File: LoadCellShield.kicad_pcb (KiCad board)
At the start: 2 copper layers, 68.6 x 53.3 mm, 34 parts, among them IC1 INA125, IC2 INA125, J1 Screw_Terminal_01x04, J2 Screw_Terminal_01x04, J7 Barrel_Jack_Switch, P1 Power, P2 Analog, P3 Digital, P4 Digital, P5 CONN_01X01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

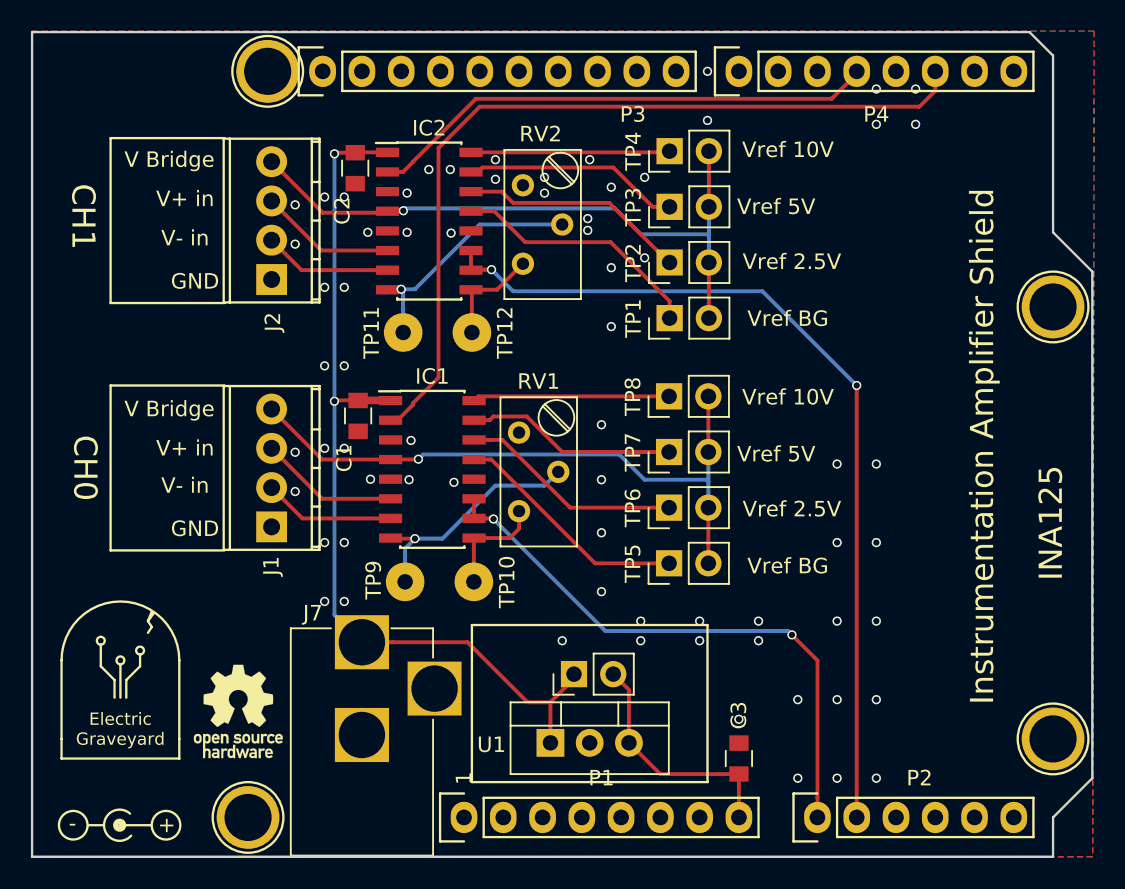
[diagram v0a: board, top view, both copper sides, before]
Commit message: Revise Layout to simplify build
Assembling these was a pain because of the 8x 2 position headers.  Squashed them so 2x 8 position ones will work.  Also some improvements to general routing.
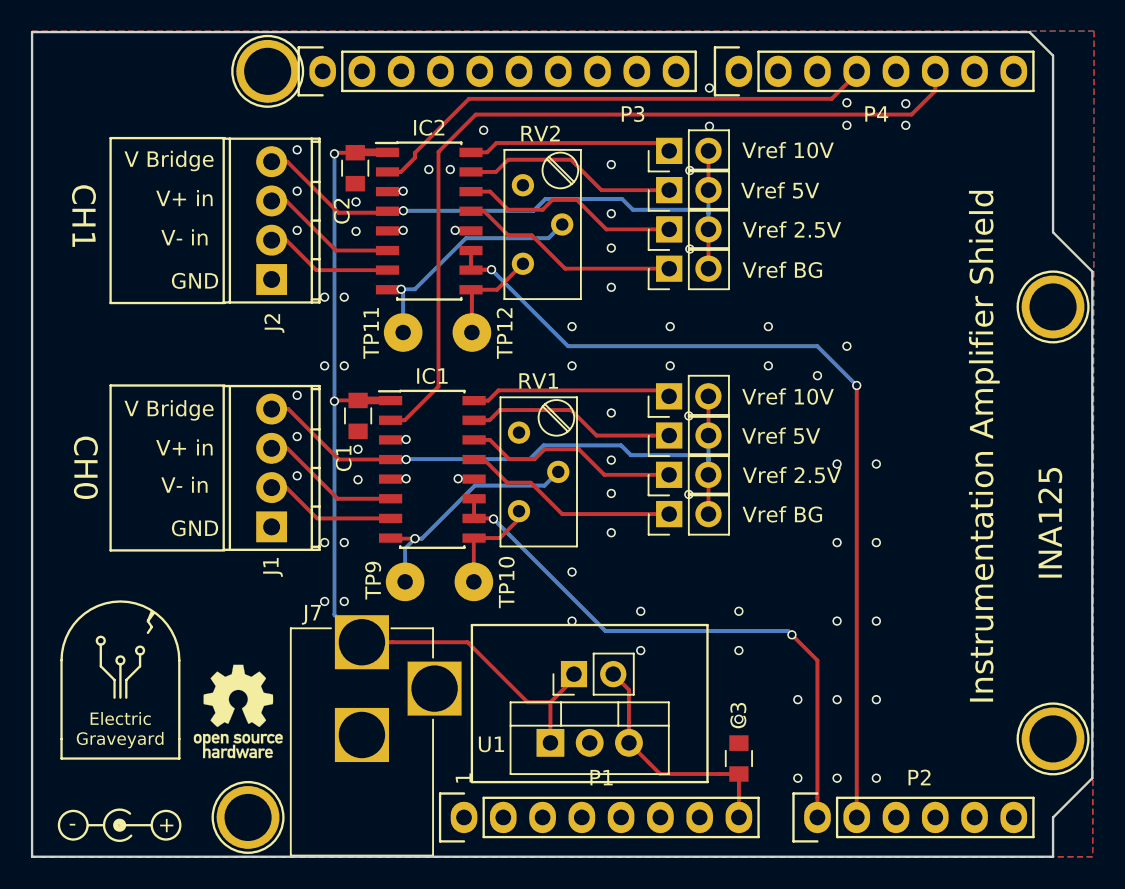
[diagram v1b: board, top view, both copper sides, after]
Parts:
- moved TP1 3.20 mm to (152.2, 88.3)
- moved TP5 3.18 mm to (152.2, 104.2)
- moved TP2 2.14 mm to (152.2, 85.8)
- moved TP6 2.12 mm to (152.2, 101.7)
- moved TP3 1.08 mm to (152.2, 83.2)
- moved TP7 1.06 mm to (152.2, 99.1)
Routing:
- net V_Bridge1: track 41.3 -> 38.2 mm
- net V_Bridge0: track 41.3 -> 39.2 mm
- net Net-(IC2-Pad13): track 16.8 -> 14.8 mm
- net Net-(IC1-Pad13): track 15.8 -> 14.5 mm
- net Net-(IC2-Pad16): track 13.3 -> 13.8 mm
- net GND: vias 68 -> 72
